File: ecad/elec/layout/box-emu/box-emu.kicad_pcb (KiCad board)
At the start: 2 copper layers, 72.5 x 63.9 mm, 58 parts

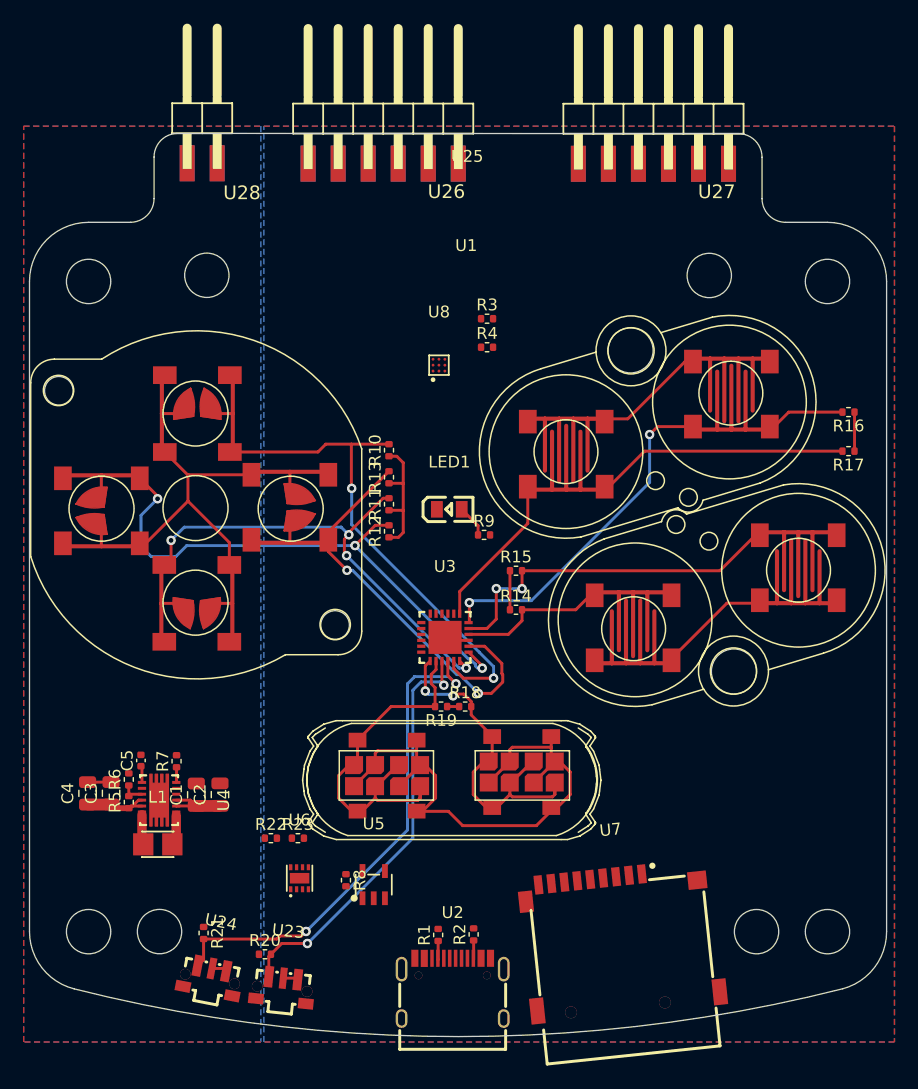
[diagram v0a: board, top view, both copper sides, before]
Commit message: update box-emu and box-3-emu borads
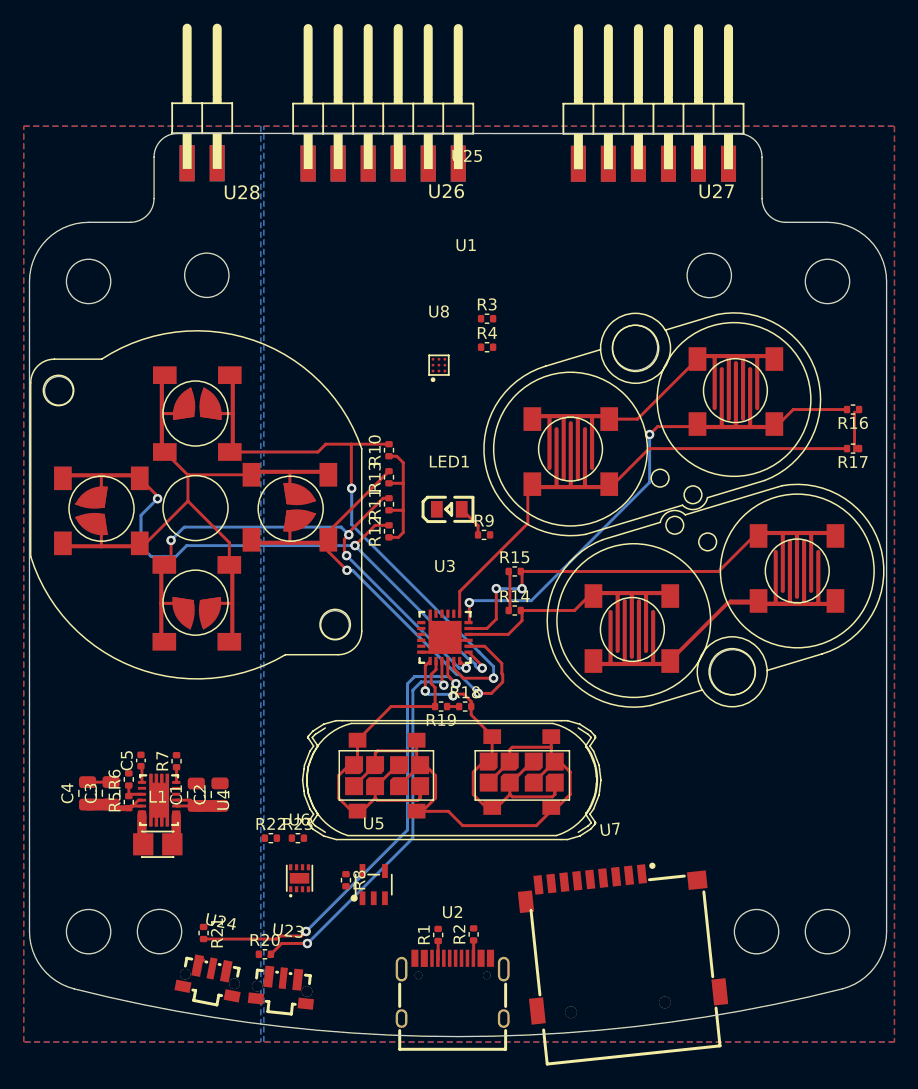
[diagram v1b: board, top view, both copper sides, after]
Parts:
- moved R16 0.44 mm to (179.7, 93.3)
- moved R17 0.44 mm to (179.7, 96.6)
- moved U17 0.44 mm to (162.8, 94.1)
- moved U18 0.44 mm to (169.8, 91.7)
- moved U19 0.44 mm to (155.8, 96.8)
- moved U14 0.12 mm to (168.0, 109.4)
- moved U15 0.12 mm to (160.9, 111.8)
- moved U16 0.12 mm to (174.9, 106.7)
- moved R14 0.12 mm to (151.0, 110.3)
- moved R15 0.12 mm to (151.0, 107.0)
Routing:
- net box-vcc: track 50.9 -> 67.8 mm
- net (no net): track 12.5 -> 0.00 mm
- net box-gnd: track 22.8 -> 27.9 mm
- net p1_3: track 42.7 -> 41.0 mm
- net p1_2: track 35.7 -> 34.0 mm

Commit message: updated footprints for the pmod headers and moved step files into .3dshapes folder
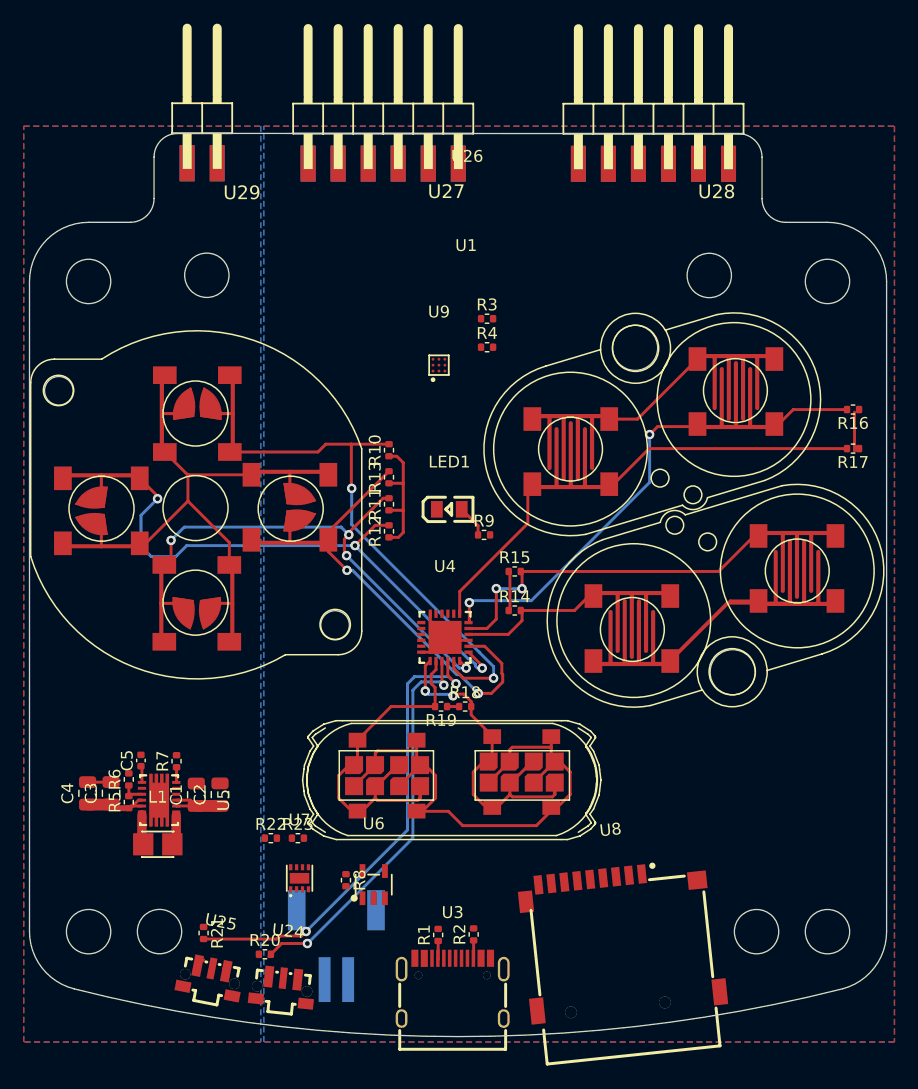
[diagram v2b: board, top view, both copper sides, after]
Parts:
- added U2: , lib:CONN-SMD_P2.00_S2B-PH-SM4-TB-LF-SN, B.Cu at (136.0, 138.5)
- R6: value 62.5mW Thick Film Resistors 50V ±100ppm/℃ ±0.5% 27.4kΩ 0402 Chip Resistor - Surface Mount ROHS -> 62.5mW Thick Film Resistors 50V ±100ppm/℃ ±1% 27.4kΩ 0402 Chip Resistor - Surface Mount ROHS
- renumbered U9 to U10, U10 to U11, U11 to U12, U12 to U13, U13 to U14, U14 to U15, U15 to U16, U16 to U17, U17 to U18, U18 to U19, U19 to U20, U20 to U21, U21 to U22, U22 to U23, U23 to U24, U24 to U25, U25 to U26, U26 to U27, U27 to U28, U28 to U29, U2 to U3, U3 to U4, U4 to U5, U5 to U6, U6 to U7, U7 to U8, U8 to U9
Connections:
- U24 pad 1: p1_2 -> box-vcc
- U24 pad 2: box-vcc -> p1_2
- U25 pad 1: p1_3 -> box-vcc
- U25 pad 2: box-vcc -> p1_3
- U4 pad 18: ad0 -> box-gnd
- U4 pad 24: ad1 -> box-gnd
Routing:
- net p1_3: track 41.0 -> 40.3 mm
- net box-vcc: track 67.8 -> 68.5 mm

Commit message: WIP fleshing out more of the design
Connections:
- U9 pad A1: (no net) -> en
- U9 pad A2: (no net) -> reg
- U9 pad A3: (no net) -> out_p
- U9 pad B1: (no net) -> in_trig
- U9 pad B2: (no net) -> sda
- U9 pad B3: (no net) -> box-gnd
- U9 pad C1: (no net) -> scl
- U9 pad C2: (no net) -> box-vcc
- U9 pad C3: (no net) -> out_m

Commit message: update layouts
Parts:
- added DS1: , lib:SOD-323_L1.8-W1.3-LS2.5-RD, F.Cu at (129.5, 122.9)
- added J1: , lib:CONN-SMD_4P-P1.00_SM04B-SRSS-TB-LF-SN, F.Cu at (176.5, 124.7)
- added U10: , Connector_PinHeader_1.00mm:PinHeader_1x02_P1.00mm_Vertical, F.Cu at (135.8, 84.8)
- renumbered U10 to U11, U11 to U12, U12 to U13, U13 to U14, U14 to U15, U15 to U16, U16 to U17, U17 to U18, U18 to U19, U19 to U20, U20 to U21, U21 to U22, U22 to U23, U23 to U24, U24 to U25, U25 to U26, U26 to U27, U27 to U28, U28 to U29, U29 to U30
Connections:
- U9 pad A3: out_p -> a
- U9 pad C3: out_m -> b

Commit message: fleshing out
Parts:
- moved R22 17.8 mm to (147.9, 132.6), turned to 90 degrees
- moved R23 16.8 mm to (149.2, 132.6), turned to -90 degrees
- moved R21 3.93 mm to (128.6, 137.9)
- moved R20 1.46 mm to (130.2, 137.9), turned to -90 degrees
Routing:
- net box.mcp73831-gnd: track 0.00 -> 56.5 mm, vias 0 -> 2
- net sda: track 0.00 -> 29.0 mm, vias 0 -> 2
- net scl: track 0.00 -> 26.3 mm
- net box-vcc: track 68.5 -> 78.8 mm
- net box-gnd: track 27.9 -> 35.9 mm
- net p1_2: track 34.0 -> 37.0 mm, vias 2 -> 3
- net p1_3: track 40.3 -> 42.7 mm
- net prog: track 0.00 -> 1.51 mm
- net battery_measurement: track 0.00 -> 1.27 mm
- added copper zone on F.Cu, net box-gnd
- added copper zone on B.Cu, net box-vcc
- removed copper zone on F.Cu, net (none)

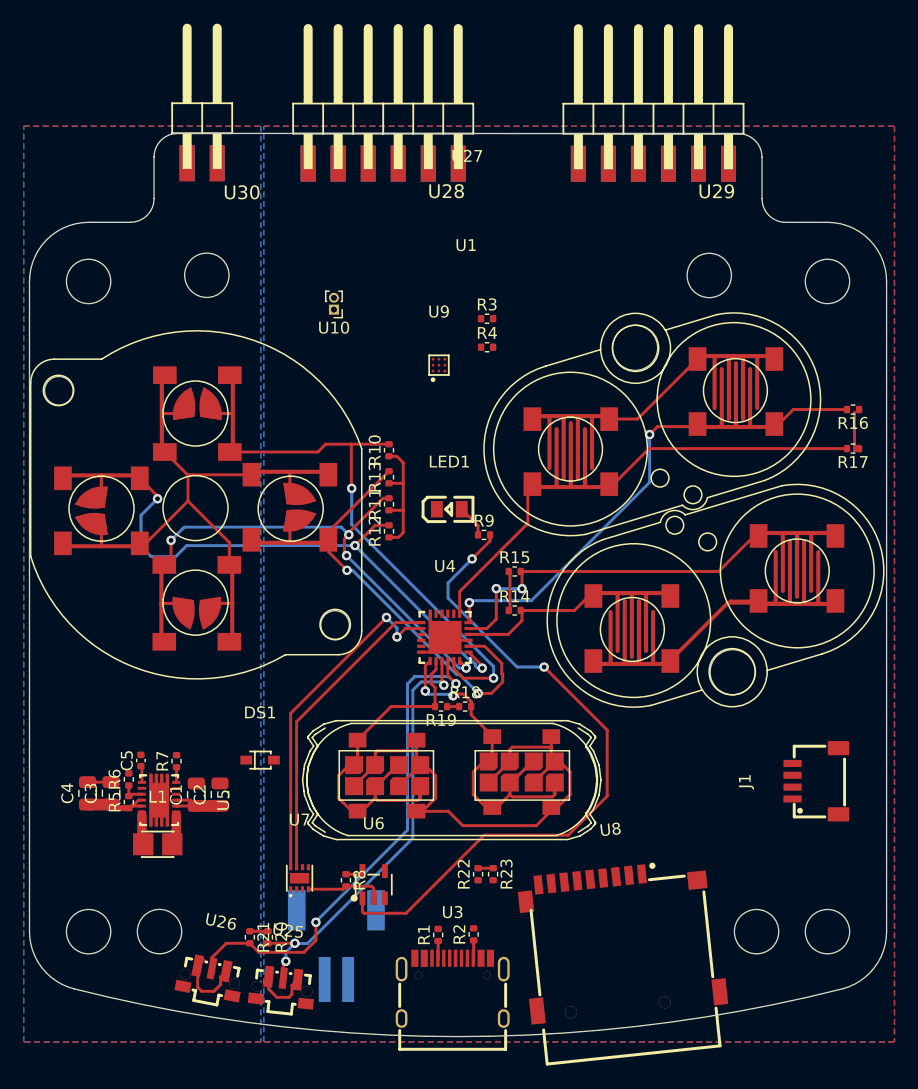
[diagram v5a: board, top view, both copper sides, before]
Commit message: change drv2605 to tssop and update box-3 connector. flesh out implemenation and wiring
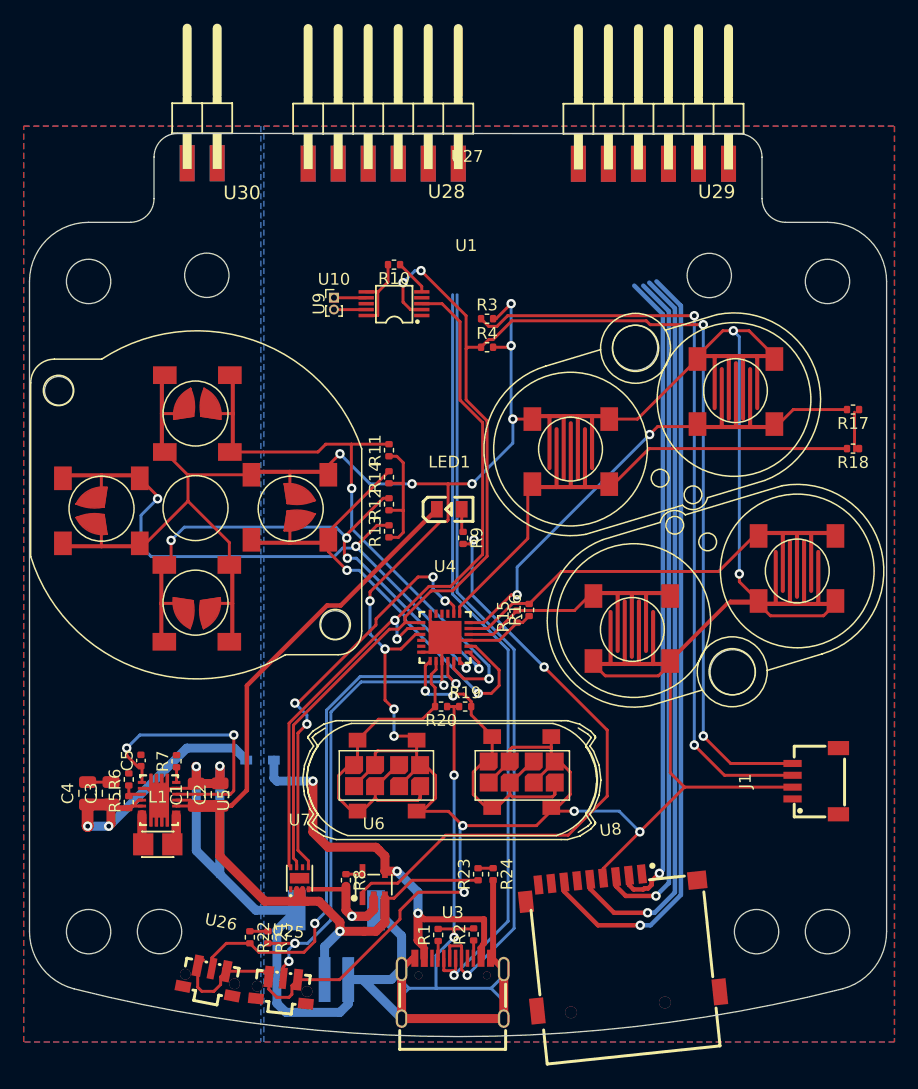
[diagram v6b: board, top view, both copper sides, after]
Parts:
- added R10: 62.5mW Thick Film Resistors 50V ±100ppm/℃ ±1% 10kΩ 0402 Chi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, lib:R0402, F.Cu at (140.8, 81.0)
- DS1: moved to B.Cu
- U9: footprint lib:DSBGA-9_L1.5-W1.5-R3-C3-P0.50-BL -> lib:VSSOP-10_L3.0-W3.0-P0.50-LS4.9-BL
- moved U9 6.44 mm to (140.8, 84.3), turned to 90 degrees
- moved R16 3.48 mm to (152.3, 110.2), turned to 90 degrees
- moved R9 1.79 mm to (146.7, 104.1), turned to -90 degrees
- moved U10 1.01 mm to (135.8, 83.8), turned to 0 degrees
- moved R15 0.55 mm to (151.2, 110.8), turned to 90 degrees
- renumbered R10 to R11, R11 to R12, R12 to R13, R13 to R14, R14 to R15, R15 to R16, R16 to R17, R17 to R18, R18 to R19, R19 to R20, R20 to R21, R21 to R22, R22 to R23, R23 to R24
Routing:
- net box-vcc: track 78.8 -> 267.3 mm, vias 0 -> 16
- net box-gnd: track 35.9 -> 172.8 mm, vias 0 -> 5
- net scl: track 26.3 -> 132.5 mm, vias 0 -> 4
- net sda: track 29.0 -> 127.3 mm, vias 2 -> 4
- net box-vcc-2: track 5.63 -> 78.5 mm, vias 0 -> 1
- net dp: track 0.00 -> 65.9 mm, vias 0 -> 1
- net miso: track 0.00 -> 65.7 mm, vias 0 -> 1
- net dm: track 0.00 -> 64.9 mm, vias 0 -> 1
- net sck: track 0.00 -> 62.0 mm, vias 0 -> 1
- net mosi: track 0.00 -> 57.5 mm, vias 0 -> 1
- net connector.pmod1-_4: track 0.00 -> 55.1 mm, vias 0 -> 3
- net cs: track 0.00 -> 55.1 mm, vias 0 -> 1
- net box-vcc-3: track 0.00 -> 38.4 mm, vias 0 -> 3
- net p1_2: track 37.0 -> 0.00 mm, vias 3 -> 0
- net p1_4: track 0.00 -> 35.4 mm, vias 0 -> 4
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
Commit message: fleshing out routing for base, box, and box-3
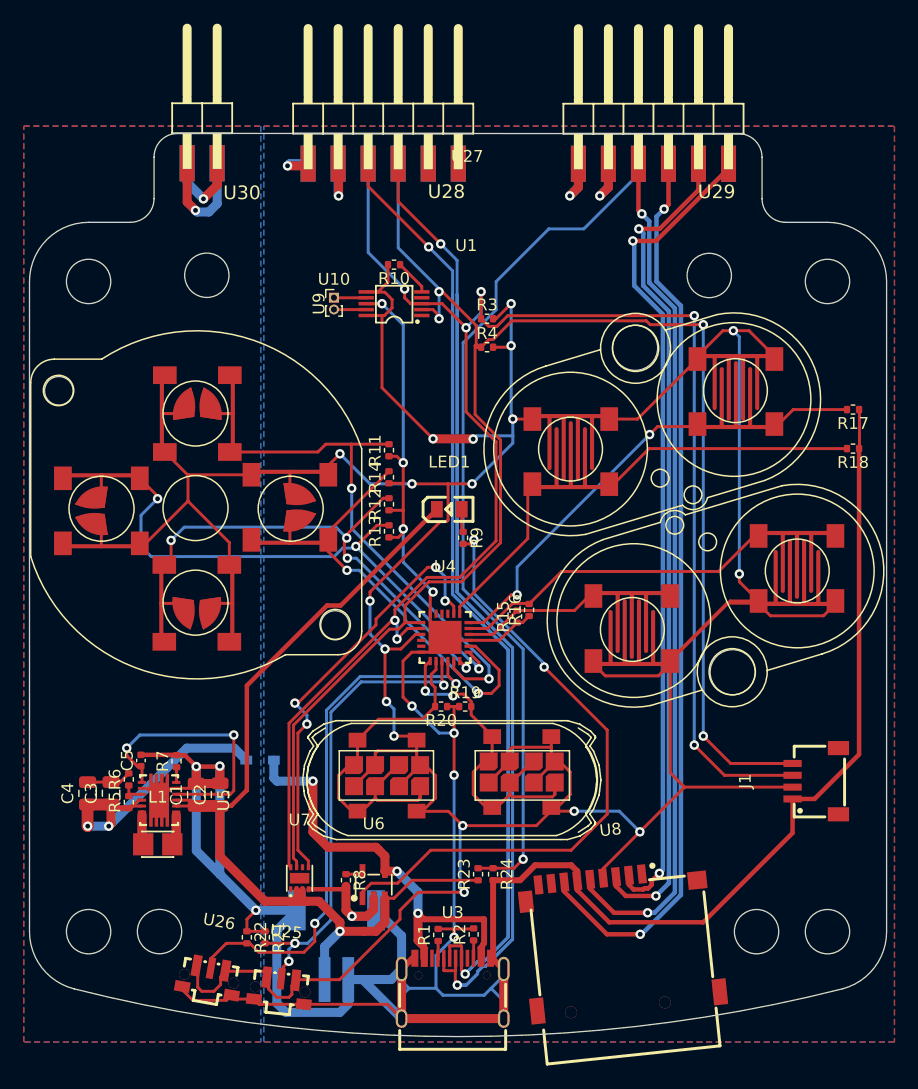
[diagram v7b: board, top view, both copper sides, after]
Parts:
- moved R22 0.25 mm to (128.4, 137.9)
- moved R21 0.25 mm to (129.9, 137.9)
- moved U25 0.18 mm to (131.2, 142.4)
- moved U26 0.07 mm to (125.2, 141.5), turned to -10 degrees
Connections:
- U25 pad 4: box.vol_up.btn.btn-_4 -> box-gnd
- U25 pad 5: box.vol_up.btn.btn-_4 -> box-gnd
- U26 pad 4: box.vol_down.btn.btn-_4 -> box-gnd
- U26 pad 5: box.vol_down.btn.btn-_4 -> box-gnd
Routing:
- net box-gnd: track 172.8 -> 341.6 mm, vias 5 -> 15
- net dm: track 64.9 -> 143.2 mm, vias 1 -> 2
- net dp: track 65.9 -> 141.0 mm, vias 1 -> 2
- net battery_measurement: track 1.27 -> 72.9 mm, vias 0 -> 1
- net connector.pmod1-_4: track 55.1 -> 0.00 mm, vias 3 -> 0
- net p1_2: track 0.00 -> 39.9 mm, vias 0 -> 3
- net box-vcc: track 267.3 -> 297.0 mm, vias 16 -> 18
- net sda: track 127.3 -> 148.9 mm, vias 4 -> 9
- net cs: track 55.1 -> 70.0 mm, vias 1 -> 2
- net mosi: track 57.5 -> 71.1 mm, vias 1 -> 2
- net miso: track 65.7 -> 76.7 mm, vias 1 -> 2
- net sck: track 62.0 -> 72.4 mm, vias 1 -> 2
- net scl: track 132.5 -> 142.6 mm
- net box-vcc-1: track 26.5 -> 33.6 mm, vias 2 -> 3
- net p1_4: track 35.4 -> 36.7 mm
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- added copper zone on B.Cu, net box-vcc-1
- removed copper zone on B.Cu, net (none)
